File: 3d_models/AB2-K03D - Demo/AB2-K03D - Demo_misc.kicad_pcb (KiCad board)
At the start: 2 copper layers, 35 parts

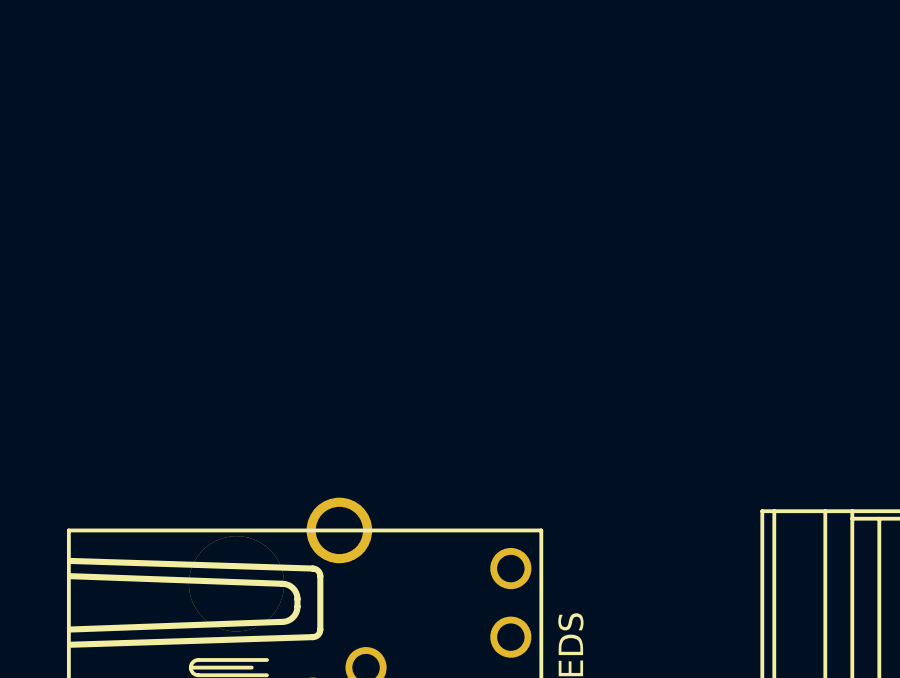
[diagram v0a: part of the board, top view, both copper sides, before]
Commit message: AB2-K03D: add encoder to misc
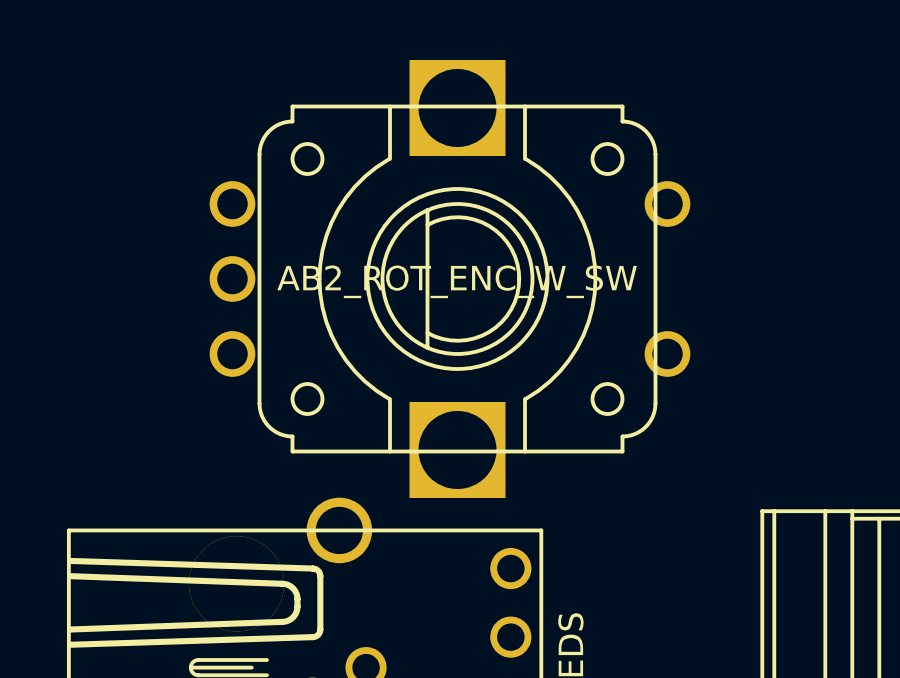
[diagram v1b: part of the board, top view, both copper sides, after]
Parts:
- added ROT_ENC1: AB2_ROT_ENC_W_SW, AB2_ROTARY_ENCODER_W_SWITCH, F.Cu at (21.6, 209.6)
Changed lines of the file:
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@@
 (kicad_pcb (version 3) (host pcbnew "(2013-07-07 BZR 4022)-stable")
   (general
-    (links 0)
-    (no_connects 0)
-    (area 8.1915 110.593012 302.9585 286.4485)
+    (links 1)
+    (no_connects 1)
+    (area 6.9215 210.1215 233.997501 286.4485)
     (thickness 1.6)
     (drawings 0)
     (tracks 0)
     (zones 0)
-    (modules 35)
-    (nets 1)
+    (modules 36)
+    (nets 5)
   )
   (page A3)
@@
   )
   (net 0 "")
+  (net 1 /R_ENCA)
+  (net 2 /R_ENCB)
+  (net 3 /R_SW+)
+  (net 4 GND)
   (net_class Default "This is the default net class."
     (clearance 0.254)
@@
     (uvia_drill 0.127)
     (add_net "")
+    (add_net /R_ENCA)
+    (add_net /R_ENCB)
+    (add_net /R_SW+)
+    (add_net GND)
   )
   (module AB2_RJ45_RA_LEDS (layer F.Cu)
@@
     )
   )
+  (module AB2_ROTARY_ENCODER_W_SWITCH (layer F.Cu)
+    (at 21.59 209.55 270)
+    (fp_text reference ROT_ENC1 (at 0 -8.89 270) (layer F.SilkS) hide
+      (effects (font (size 0.8128 0.8128) (thickness 0.0762)))
+    )
+    (fp_text value AB2_ROT_ENC_W_SW (at 0 0 360) (layer F.SilkS)
+      (effects (font (size 0.8128 0.8128) (thickness 0.0762)))
+    )
+    (fp_arc (start 0 0) (end 0 4.6) (angle 60) (layer F.SilkS) (width 0.127))
+    (fp_arc (start 0 0) (end 0 4.6) (angle -60) (layer F.SilkS) (width 0.127))
+    (fp_arc (start 0 0) (end 0 -4.6) (angle 60) (layer F.SilkS) (width 0.127))
+    (fp_arc (start 0 0) (end 0 -4.6) (angle -60) (layer F.SilkS) (width 0.127))
+    (fp_circle (center 4 5) (end 4 4.5) (layer F.SilkS) (width 0.127))
+    (fp_circle (center -4 5) (end -4 4.5) (layer F.SilkS) (width 0.127))
+    (fp_circle (center 4 -5) (end 4 -5.5) (layer F.SilkS) (width 0.127))
+    (fp_circle (center -4 -5) (end -4 -5.5) (layer F.SilkS) (width 0.127))
+    (fp_line (start 5.75 -2.25) (end 4 -2.25) (layer F.SilkS) (width 0.127))
+    (fp_line (start -5.75 -2.25) (end -4 -2.25) (layer F.SilkS) (width 0.127))
+    (fp_line (start 5.75 2.25) (end 4 2.25) (layer F.SilkS) (width 0.127))
+    (fp_line (start -5.75 2.25) (end -4 2.25) (layer F.SilkS) (width 0.127))
+    (fp_arc (start 4.15 5.5) (end 5.25 5.5) (angle 90) (layer F.SilkS) (width 0.127))
+    (fp_arc (start -4.15 5.5) (end -4.15 6.6) (angle 90) (layer F.SilkS) (width 0.127))
+    (fp_arc (start -4.15 -5.5) (end -5.25 -5.5) (angle 90) (layer F.SilkS) (width 0.127))
+    (fp_arc (start 4.15 -5.5) (end 4.15 -6.6) (angle 90) (layer F.SilkS) (width 0.127))
+    (fp_line (start 5.75 -5.5) (end 5.25 -5.5) (layer F.SilkS) (width 0.127))
+    (fp_line (start -5.75 -5.5) (end -5.25 -5.5) (layer F.SilkS) (width 0.127))
+    (fp_line (start -5.75 5.5) (end -5.25 5.5) (layer F.SilkS) (width 0.127))
+    (fp_line (start 5.75 5.5) (end 5.25 5.5) (layer F.SilkS) (width 0.127))
+    (fp_line (start -4.15 6.6) (end 4.15 6.6) (layer F.SilkS) (width 0.127))
+    (fp_line (start -4.15 -6.6) (end 4.15 -6.6) (layer F.SilkS) (width 0.127))
+    (fp_line (start 5.75 -5.5) (end 5.75 5.5) (layer F.SilkS) (width 0.127))
+    (fp_line (start -5.75 -5.5) (end -5.75 5.5) (layer F.SilkS) (width 0.127))
+    (fp_line (start -2.3 1) (end 2.3 1) (layer F.SilkS) (width 0.127))
+    (fp_circle (center 0 0) (end 0 -3) (layer F.SilkS) (width 0.127))
+    (fp_circle (center 0 0) (end 0 -2.5) (layer F.SilkS) (width 0.127))
+    (fp_arc (start 0 0) (end 1.8 1) (angle -120) (layer F.SilkS) (width 0.127))
+    (fp_arc (start 0 0) (end -1.8 1) (angle 120) (layer F.SilkS) (width 0.127))
+    (pad 1 thru_hole circle (at -2.5 7.5 270) (size 1.524 1.524) (drill 1.016)
+      (layers *.Cu *.Mask F.SilkS)
+      (net 1 /R_ENCA)
+    )
+    (pad 2 thru_hole circle (at 0 7.5 270) (size 1.524 1.524) (drill 1.016)
+      (layers *.Cu *.Mask F.SilkS)
+      (net 4 GND)
+    )
+    (pad 3 thru_hole circle (at 2.5 7.5 270) (size 1.524 1.524) (drill 1.016)
+      (layers *.Cu *.Mask F.SilkS)
+      (net 2 /R_ENCB)
+    )
+    (pad 4 thru_hole circle (at 2.5 -7 270) (size 1.524 1.524) (drill 1.016)
+      (layers *.Cu *.Mask F.SilkS)
+      (net 3 /R_SW+)
+    )
+    (pad 6 thru_hole circle (at -2.5 -7 270) (size 1.524 1.524) (drill 1.016)
+      (layers *.Cu *.Mask F.SilkS)
+      (net 4 GND)
+    )
+    (pad 7 thru_hole rect (at -5.7 0 270) (size 3.2 3.2) (drill 2.6)
+      (layers *.Cu *.Mask F.SilkS)
+    )
+    (pad 7 thru_hole rect (at 5.7 0 270) (size 3.2 3.2) (drill 2.6)
+      (layers *.Cu *.Mask F.SilkS)
+    )
+    (model ../3d_models/ab2_input_devices/AB2_ROT_ENC_W_SW.wrl
+      (at (xyz 0 0 0))
+      (scale (xyz 0.01573 0.01573 0.01573))
+      (rotate (xyz 0 0 180))
+    )
+  )

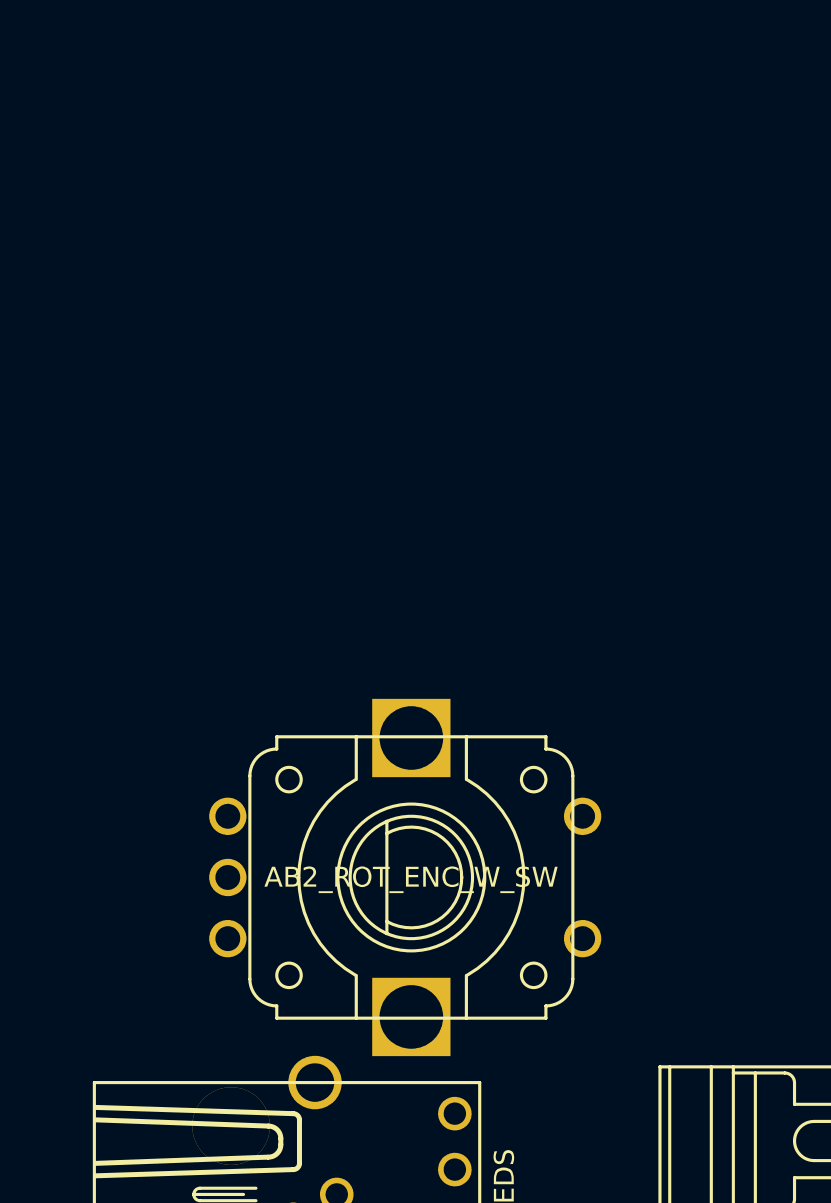
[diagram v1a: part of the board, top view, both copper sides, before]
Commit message: 3d_models: AB2-K03D: add 90' 4mm banana jack
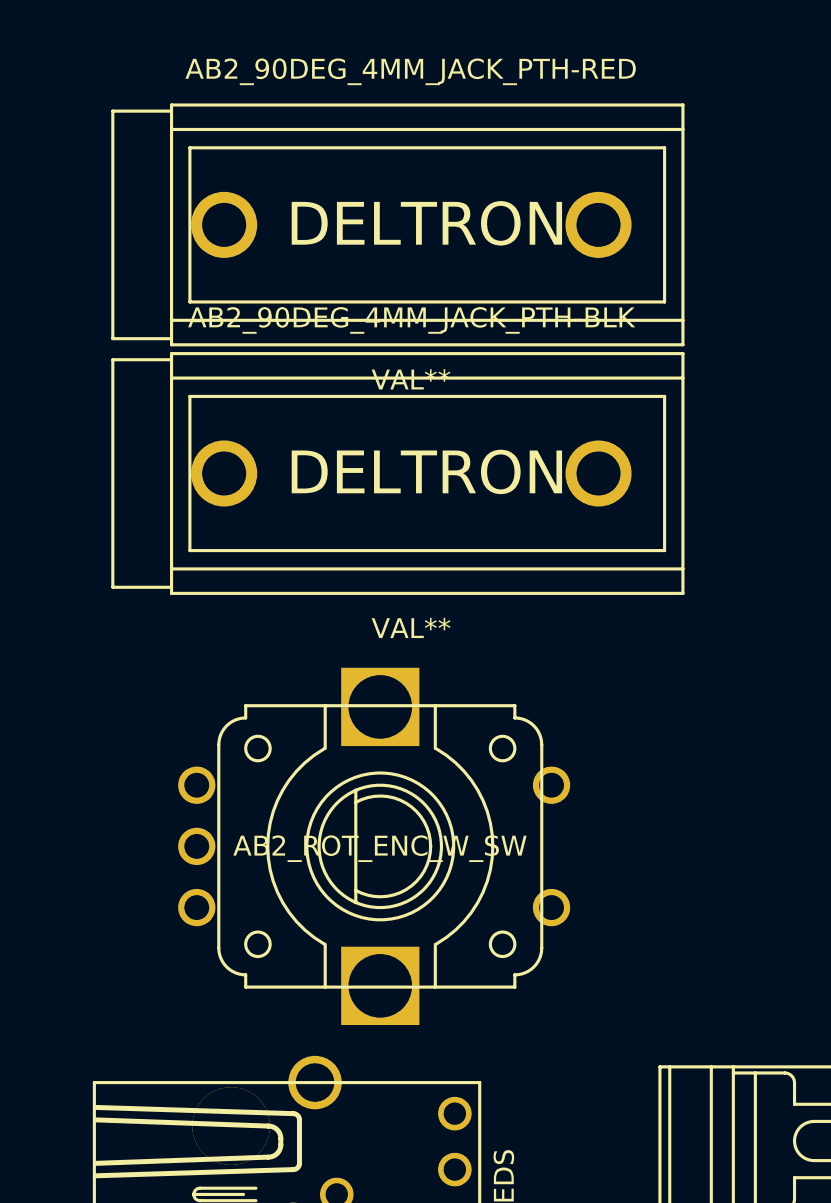
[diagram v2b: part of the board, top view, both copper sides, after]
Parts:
- added AB2_90DEG_4MM_JACK_PTH-BLK: VAL**, AB2_90DEG_4MM_JACK_PTH-BLK, F.Cu at (21.6, 193.0)
- added AB2_90DEG_4MM_JACK_PTH-RED: VAL**, AB2_90DEG_4MM_JACK_PTH-RED, F.Cu at (21.6, 182.9)
- moved ROT_ENC1 1.80 mm to (20.3, 208.3)
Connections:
- ROT_ENC1 pad 1: /R_ENCA -> (no net)
- ROT_ENC1 pad 2: GND -> (no net)
- ROT_ENC1 pad 3: /R_ENCB -> (no net)
- ROT_ENC1 pad 4: /R_SW+ -> (no net)
- ROT_ENC1 pad 6: GND -> (no net)
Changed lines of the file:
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@@
 (kicad_pcb (version 3) (host pcbnew "(2013-07-07 BZR 4022)-stable")
   (general
-    (links 1)
-    (no_connects 1)
-    (area 6.9215 210.1215 233.997501 286.4485)
+    (links 0)
+    (no_connects 0)
+    (area 6.9215 201.333258 233.997501 286.4485)
     (thickness 1.6)
     (drawings 0)
     (tracks 0)
     (zones 0)
-    (modules 36)
-    (nets 5)
+    (modules 38)
+    (nets 1)
   )
   (page A3)
@@
   )
   (net 0 "")
-  (net 1 /R_ENCA)
-  (net 2 /R_ENCB)
-  (net 3 /R_SW+)
-  (net 4 GND)
   (net_class Default "This is the default net class."
     (clearance 0.254)
@@
     (uvia_drill 0.127)
     (add_net "")
-    (add_net /R_ENCA)
-    (add_net /R_ENCB)
-    (add_net /R_SW+)
-    (add_net GND)
   )
   (module AB2_RJ45_RA_LEDS (layer F.Cu)
@@
   )
   (module AB2_ROTARY_ENCODER_W_SWITCH (layer F.Cu)
-    (at 21.59 209.55 270)
+    (at 20.32 208.28 270)
     (fp_text reference ROT_ENC1 (at 0 -8.89 270) (layer F.SilkS) hide
       (effects (font (size 0.8128 0.8128) (thickness 0.0762)))
@@
     (pad 1 thru_hole circle (at -2.5 7.5 270) (size 1.524 1.524) (drill 1.016)
       (layers *.Cu *.Mask F.SilkS)
-      (net 1 /R_ENCA)
     )
     (pad 2 thru_hole circle (at 0 7.5 270) (size 1.524 1.524) (drill 1.016)
       (layers *.Cu *.Mask F.SilkS)
-      (net 4 GND)
     )
     (pad 3 thru_hole circle (at 2.5 7.5 270) (size 1.524 1.524) (drill 1.016)
       (layers *.Cu *.Mask F.SilkS)
-      (net 2 /R_ENCB)
     )
     (pad 4 thru_hole circle (at 2.5 -7 270) (size 1.524 1.524) (drill 1.016)
       (layers *.Cu *.Mask F.SilkS)
-      (net 3 /R_SW+)
     )
     (pad 6 thru_hole circle (at -2.5 -7 270) (size 1.524 1.524) (drill 1.016)
       (layers *.Cu *.Mask F.SilkS)
-      (net 4 GND)
     )
     (pad 7 thru_hole rect (at -5.7 0 270) (size 3.2 3.2) (drill 2.6)
@@
       (rotate (xyz 0 0 180))
     )
+  )
+  (module AB2_90DEG_4MM_JACK_PTH-BLK (layer F.Cu)
+    (at 21.59 193.04)
+    (fp_text reference AB2_90DEG_4MM_JACK_PTH-BLK (at 0 -6.35) (layer F.SilkS)
+      (effects (font (size 0.8128 0.8128) (thickness 0.0762)))
+    )
+    (fp_text value VAL** (at 0 6.35) (layer F.SilkS)
+      (effects (font (size 0.8128 0.8128) (thickness 0.0762)))
+    )
+    (fp_line (start -9.05 -3.15) (end 10.35 -3.15) (layer F.SilkS) (width 0.127))
+    (fp_line (start 10.35 -3.15) (end 10.35 3.15) (layer F.SilkS) (width 0.127))
+    (fp_line (start 10.35 3.15) (end -9.05 3.15) (layer F.SilkS) (width 0.127))
+    (fp_line (start -9.05 3.15) (end -9.05 -3.15) (layer F.SilkS) (width 0.127))
+    (fp_line (start -9.8 3.9) (end 11.1 3.9) (layer F.SilkS) (width 0.127))
+    (fp_line (start -9.8 -3.9) (end 11.1 -3.9) (layer F.SilkS) (width 0.127))
+    (fp_text user DELTRON (at 0.635 0) (layer F.SilkS)
+      (effects (font (size 1.75 1.75) (thickness 0.2)))
+    )
+    (fp_line (start -9.8 -4.65) (end -12.2 -4.65) (layer F.SilkS) (width 0.127))
+    (fp_line (start -12.2 -4.65) (end -12.2 4.65) (layer F.SilkS) (width 0.127))
+    (fp_line (start -12.2 4.65) (end -9.8 4.65) (layer F.SilkS) (width 0.127))
+    (fp_line (start -9.8 -4.9) (end -9.8 4.9) (layer F.SilkS) (width 0.127))
+    (fp_line (start -9.8 4.9) (end 11.1 4.9) (layer F.SilkS) (width 0.127))
+    (fp_line (start 11.1 4.9) (end 11.1 -4.9) (layer F.SilkS) (width 0.127))
+    (fp_line (start 11.1 -4.9) (end -9.8 -4.9) (layer F.SilkS) (width 0.127))
+    (pad 1 thru_hole circle (at -7.65 0) (size 2.7 2.7) (drill 1.8)
+      (layers *.Cu *.Mask F.SilkS)
+    )
+    (pad 1 thru_hole circle (at 7.65 0) (size 2.7 2.7) (drill 1.8)
+      (layers *.Cu *.Mask F.SilkS)
+    )
+    (model ../3d_models/ab2_power/AB2_90DEG_4MM_JACK_PTH-BLK.wrl
+      (at (xyz 0 0 0))
+      (scale (xyz 0.3937 0.3937 0.3937))
+      (rotate (xyz 0 0 180))
+    )
+  )
+  (module AB2_90DEG_4MM_JACK_PTH-RED (layer F.Cu)
+    (at 21.59 182.88)
+    (fp_text reference AB2_90DEG_4MM_JACK_PTH-RED (at 0 -6.35) (layer F.SilkS)
+      (effects (font (size 0.8128 0.8128) (thickness 0.0762)))
+    )
+    (fp_text value VAL** (at 0 6.35) (layer F.SilkS)
+      (effects (font (size 0.8128 0.8128) (thickness 0.0762)))
+    )
+    (fp_line (start -9.05 -3.15) (end 10.35 -3.15) (layer F.SilkS) (width 0.127))
+    (fp_line (start 10.35 -3.15) (end 10.35 3.15) (layer F.SilkS) (width 0.127))
+    (fp_line (start 10.35 3.15) (end -9.05 3.15) (layer F.SilkS) (width 0.127))
+    (fp_line (start -9.05 3.15) (end -9.05 -3.15) (layer F.SilkS) (width 0.127))
+    (fp_line (start -9.8 3.9) (end 11.1 3.9) (layer F.SilkS) (width 0.127))
+    (fp_line (start -9.8 -3.9) (end 11.1 -3.9) (layer F.SilkS) (width 0.127))
+    (fp_text user DELTRON (at 0.635 0) (layer F.SilkS)
+      (effects (font (size 1.75 1.75) (thickness 0.2)))
+    )
+    (fp_line (start -9.8 -4.65) (end -12.2 -4.65) (layer F.SilkS) (width 0.127))
+    (fp_line (start -12.2 -4.65) (end -12.2 4.65) (layer F.SilkS) (width 0.127))
+    (fp_line (start -12.2 4.65) (end -9.8 4.65) (layer F.SilkS) (width 0.127))
+    (fp_line (start -9.8 -4.9) (end -9.8 4.9) (layer F.SilkS) (width 0.127))
+    (fp_line (start -9.8 4.9) (end 11.1 4.9) (layer F.SilkS) (width 0.127))
+    (fp_line (start 11.1 4.9) (end 11.1 -4.9) (layer F.SilkS) (width 0.127))
+    (fp_line (start 11.1 -4.9) (end -9.8 -4.9) (layer F.SilkS) (width 0.127))
+    (pad 1 thru_hole circle (at -7.65 0) (size 2.7 2.7) (drill 1.8)
+      (layers *.Cu *.Mask F.SilkS)
+    )
+    (pad 1 thru_hole circle (at 7.65 0) (size 2.7 2.7) (drill 1.8)
+      (layers *.Cu *.Mask F.SilkS)
+    )
+    (model ../3d_models/ab2_power/AB2_90DEG_4MM_JACK_PTH-RED.wrl
+      (at (xyz 0 0 0))
+      (scale (xyz 0.3937 0.3937 0.3937))
+      (rotate (xyz 0 0 180))
+    )
